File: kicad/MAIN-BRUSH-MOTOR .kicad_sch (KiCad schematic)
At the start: 9 parts, among them J11 MAIN BRUSH, U20 DRV8870DDAR

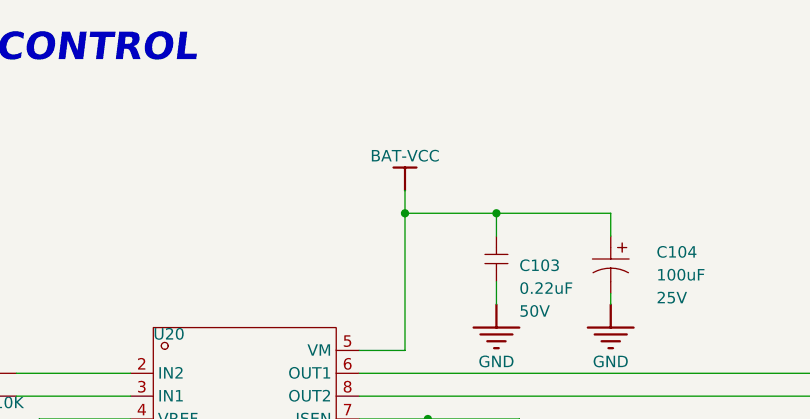
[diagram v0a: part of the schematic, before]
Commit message: RTC clock, signal integrity
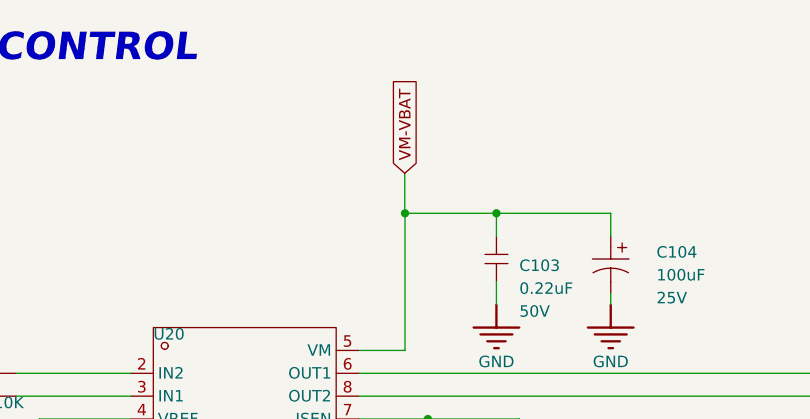
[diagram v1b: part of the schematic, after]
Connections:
- net BAT-VCC renamed VM-VBAT
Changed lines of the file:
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@@
+	)
+	(junction
+		(at 254.026 152.4)
+		(diameter 0)
+		(color 0 0 0 0)
 	)
 	(junction
@@
 	)
 	(junction
-		(at 254.026 152.4)
-		(diameter 0)
-		(color 0 0 0 0)
-	)
-	(junction
 		(at 264.186 152.4)
 		(diameter 0)
@@
 	(wire
 		(pts
-			(xy 254.026 149.86) (xy 254.026 152.4)
+			(xy 254 147.955) (xy 254 152.4)
 		)
 		(stroke
@@
 	(wire
 		(pts
+			(xy 254 152.4) (xy 254.026 152.4)
+		)
+		(stroke
+			(width 0)
+			(type default)
+		)
+	)
+	(wire
+		(pts
 			(xy 325.12 180.34) (xy 325.12 182.88)
 		)
@@
 			(width 0)
 			(type default)
+		)
+	)
+	(global_label "VM-VBAT"
+		(shape input)
+		(at 254 147.955 90)
+		(fields_autoplaced yes)
+		(effects
+			(font
+				(size 1.27 1.27)
+			)
+			(justify left)
+		)
+		(property "Intersheetrefs" "${INTERSHEET_REFS}"
+			(at 254 136.4426 90)
+			(hide yes)
+			(show_name no)
+			(do_not_autoplace no)
+			(effects
+				(font
+					(size 1.27 1.27)
+				)
+				(justify left)
+			)
 		)
 	)
@@
 					(unit 1)
 				)
-			)
-		)
-	)
-	(symbol
-		(lib_id "oomwoo-kicad-altium-import:BAT-VCC_BAR")
-		(at 254.026 149.86 180)
-		(unit 1)
-		(body_style 1)
-		(exclude_from_sim no)
-		(in_bom yes)
-		(on_board yes)
-		(in_pos_files yes)
-		(dnp no)
-		(property "Reference" "#PWR0597"
-			(at 254.026 149.86 0)
-			(hide yes)
-			(show_name no)
-			(do_not_autoplace no)
-			(effects
-				(font
-					(size 1.27 1.27)
-				)
-			)
-		)
-		(property "Value" "BAT-VCC"
-			(at 254.026 146.05 0)
-			(show_name no)
-			(do_not_autoplace no)
-			(effects
-				(font
-					(size 1.27 1.27)
-				)
-			)
-		)
-		(property "Footprint" ""
-			(at 254.026 149.86 0)
-			(show_name no)
-			(do_not_autoplace no)
-			(effects
-				(font
-					(size 1.27 1.27)
-				)
-			)
-		)
-		(property "Datasheet" ""
-			(at 254.026 149.86 0)
-			(show_name no)
-			(do_not_autoplace no)
-			(effects
-				(font
-					(size 1.27 1.27)
-				)
-			)
-		)
-		(property "Description" ""
-			(at 254.026 149.86 0)
-			(show_name no)
-			(do_not_autoplace no)
-			(effects
-				(font
-					(size 1.27 1.27)
-				)
-			)
-		)
-		(pin ""
-		)
-		(instances
-			(project "oomwoo-kicad"
-				(path "/dbcfb655-8d45-4808-9a74-2a0eb03372e8/d2575d7d-1146-4d18-8245-44d2d65fb93f"
-					(reference "#PWR0597")
-					(unit 1)
-				)
